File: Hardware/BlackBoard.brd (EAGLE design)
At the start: 68.6 x 53.3 mm, 78 parts, among them IC3 LM1117, J2 ISP, J3 POWER_JACKSUPER_BOMB_DIGITY, J5 USB C, Q1 1.1A/60V/600mΩ, Q2 310mA/60V/1.6Ω, Q3 310mA/60V/1.6Ω, U3 AP2112-3.3V, U4 ATMEGA328P_TQFP, U5 CH340C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

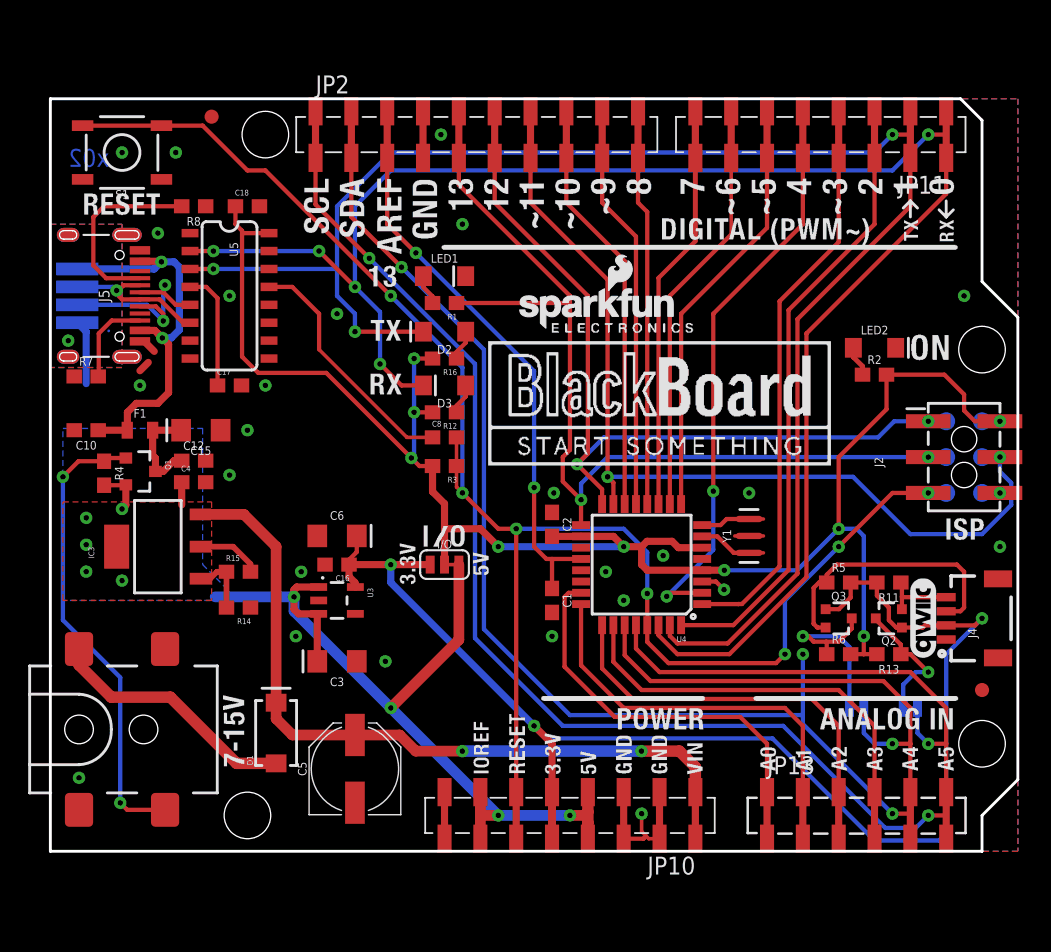
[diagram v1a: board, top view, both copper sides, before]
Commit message: Swap to larger PTC. Correct connection to IOREF.
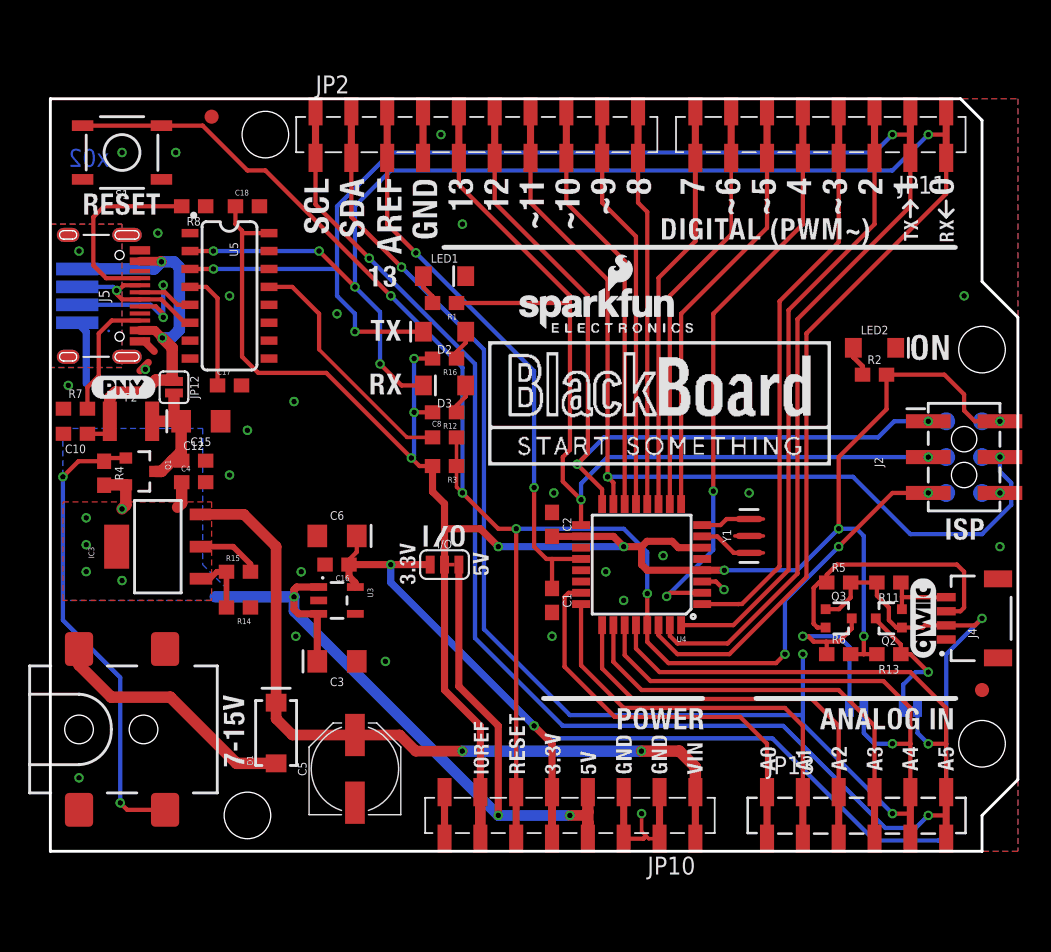
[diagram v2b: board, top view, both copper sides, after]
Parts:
- removed F1: 6V 0.5A, SparkFun-Fuses:0805
- added F2: 6V_2A, SparkFun-Fuses:1210
- added JP12: (no value), SparkFun-Jumpers:SMT-JUMPER_2_NO_SILK
- added U$13: (no value), buzzard_labels:PNY0
- J4: device SparkFun-Connectors:1X04_1MM_RA -> SparkFun-Connectors:JST04_1MM_RA
- moved R7 2.41 mm to (1.78, 31.4)
- moved C10 0.80 mm to (1.78, 29.6)
- moved C15 0.64 mm to (10.7, 30.5)
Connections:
- net 5V: no longer JP10.7A, JP10.7B
- net USBVCC: now also F2.2, JP12.2; no longer F1.2
- net VCC: now also JP10.7A, JP10.7B
- net VUSB: now also F2.1, JP12.1; no longer F1.1
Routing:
- net VCC: track 123.6 -> 144.1 mm
- net CC2: track 6.36 -> 8.97 mm
- net 5V: track 73.8 -> 76.3 mm, vias 9 -> 8
- net USBVCC: track 7.20 -> 9.50 mm
- net VUSB: track 27.7 -> 29.4 mm
- net D+: track 16.0 -> 15.4 mm
- net GND: track 12.9 -> 12.6 mm, vias 26 -> 27

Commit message: Adding panel
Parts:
- F2: value 6V_2A -> 6V/2A
- moved U$12 0.92 mm to (5.46, 42.0)
- moved U$11 0.85 mm to (5.46, 36.7)
- moved U$10 0.28 mm to (5.46, 40.3)
- moved U$2 0.25 mm to (5.59, 38.5)
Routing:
- net 5V: track 76.3 -> 76.8 mm
- net GND: track 12.6 -> 12.2 mm, vias 27 -> 42
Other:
- board text added: "x03"
- board text removed: "x02"

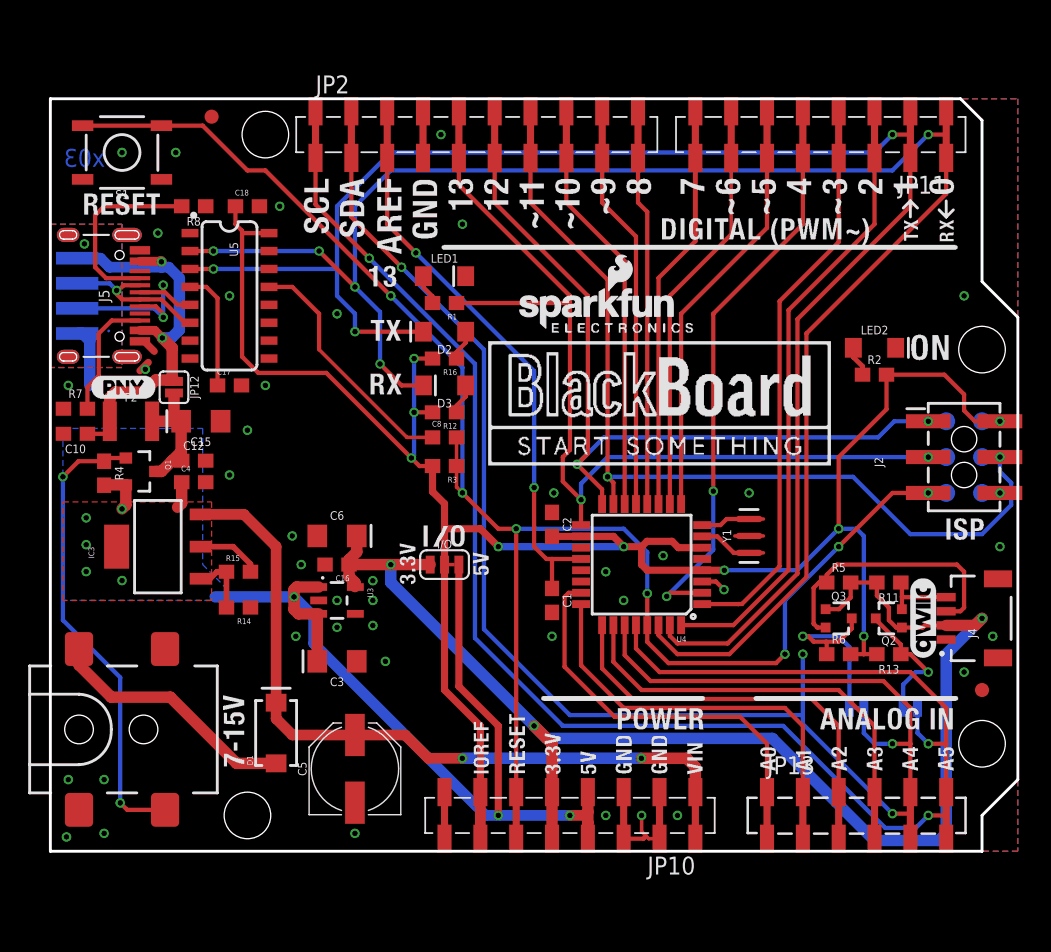
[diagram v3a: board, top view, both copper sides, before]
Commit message: Add switch for IO voltage. Add PTH holes.
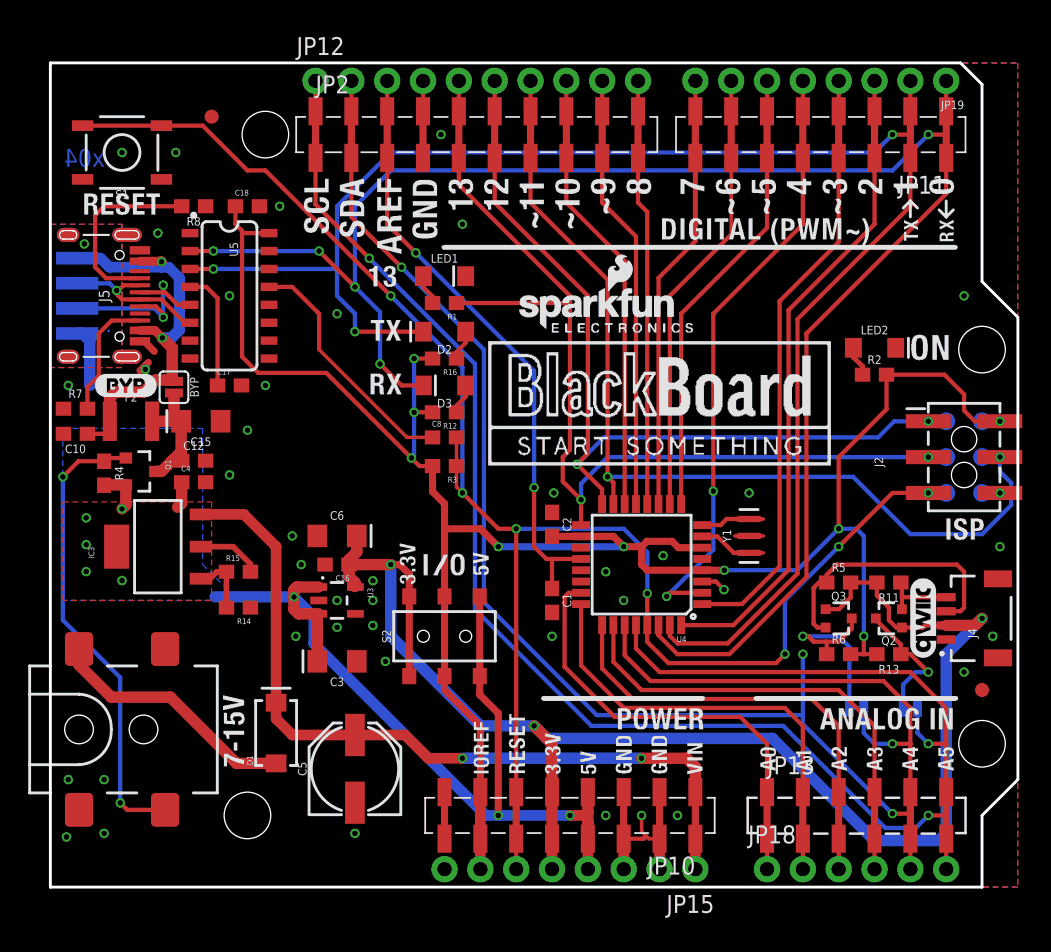
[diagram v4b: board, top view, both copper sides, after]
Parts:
- removed I/O: (no value), SparkFun-Jumpers:SMT-JUMPER_3_1-NC_TRACE_SILK
- removed U$13: (no value), buzzard_labels:PNY0
- added BYP: JUMPER-SMT_2_NO_SILK, SparkFun-Jumpers:SMT-JUMPER_2_NO_SILK
- added JP15: (no value), SparkFun-Connectors:1X08_NO_SILK@1
- added JP18: (no value), SparkFun-Connectors:1X06_NO_SILK@1
- added JP19: (no value), SparkFun-Connectors:1X08_NO_SILK
- added S2: (no value), SparkFun-Switches:SWITCH_DPDT_SMD_AYZ0202
- added U$68: (no value), buzzard_labels (13):BYP0
- D3: value Yellow -> YELLOW
- FRAME1: value FRAME-LETTER -> FRAME-LEDGER
- J4: value (none) -> QWIIC_RIGHT_ANGLE
- JP10, JP11: device SparkFun-Connectors:1X08_SMD_COMBINED -> SparkFun-Connectors:1X08_SMD_COMBINED@1
- JP12: value (none) -> M10NO_SILK; device SparkFun-Jumpers:SMT-JUMPER_2_NO_SILK -> SparkFun-Connectors:1X10_NO_SILK
- QW1, QW2: value (none) -> JUMPER-SMT_2_NC_TRACE_SILK
- moved JP12 23.9 mm to (18.8, 54.6), turned to 0 degrees
- moved FRAME1 2.54 mm to (-5.08, -35.6)
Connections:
- removed net AD0: JP13.1A, JP13.1B, U4.23
- removed net AD1: JP13.2A, JP13.2B, U4.24
- removed net AD2: JP13.3A, JP13.3B, U4.25
- removed net AD3: JP13.4A, JP13.4B, U4.26
- removed net AD4/SDA: JP13.5A, JP13.5B, JP2.2A, JP2.2B, QW2.1, U4.27
- removed net AD5/SCL: JP13.6A, JP13.6B, JP2.1A, JP2.1B, QW1.1, U4.28
- removed net IO2: JP11.3A, JP11.3B, U4.32
- removed net IO3: JP11.4A, JP11.4B, U4.1
- removed net IO4: JP11.5A, JP11.5B, U4.2
- removed net IO5: JP11.6A, JP11.6B, U4.9
- removed net IO6: JP11.7A, JP11.7B, U4.10
- removed net IO7: JP11.8A, JP11.8B, U4.11
- removed net IO8: JP2.10A, JP2.10B, U4.12
- removed net IO9: JP2.9A, JP2.9B, U4.13
- removed net RESET: C8.2, J2.5, JP10.6A, JP10.6B, R3.1, S1.3, S1.4, TP6.P$1, U4.29
- removed net SS: JP2.8A, JP2.8B, U4.14
- new net !RESET: C8.2, J2.5, JP10.6A, JP10.6B, JP15.6, R3.1, S1.3, S1.4, TP6.P$1, U4.29
- new net A0: JP13.1A, JP13.1B, JP18.1, U4.23
- new net A1: JP13.2A, JP13.2B, JP18.2, U4.24
- new net A2: JP13.3A, JP13.3B, JP18.3, U4.25
- new net A3: JP13.4A, JP13.4B, JP18.4, U4.26
- new net A4/SDA: JP12.2, JP13.5A, JP13.5B, JP18.5, JP2.2A, JP2.2B, QW2.1, U4.27
- new net A5/SCL: JP12.1, JP13.6A, JP13.6B, JP18.6, JP2.1A, JP2.1B, QW1.1, U4.28
- new net D10: JP12.8, JP2.8A, JP2.8B, U4.14
- new net D2: JP11.3A, JP11.3B, JP19.3, U4.32
- new net D3: JP11.4A, JP11.4B, JP19.4, U4.1
- new net D4: JP11.5A, JP11.5B, JP19.5, U4.2
- new net D5: JP11.6A, JP11.6B, JP19.6, U4.9
- new net D6: JP11.7A, JP11.7B, JP19.7, U4.10
- new net D7: JP11.8A, JP11.8B, JP19.8, U4.11
- new net D8: JP12.10, JP2.10A, JP2.10B, U4.12
- new net D9: JP12.9, JP2.9A, JP2.9B, U4.13
- net 3.3V: now also JP15.5, S2.1, S2.4; no longer I/O.1
- net 5V: now also JP15.4, S2.3, S2.6; no longer I/O.3
- net AREF: now also JP12.3
- net GND: now also JP12.4, JP15.2, JP15.3
- net MISO: now also JP12.6
- net MOSI: now also JP12.7
- net RX-I: now also JP19.1
- net SCK: now also JP12.5
- net TX-O: now also JP19.2
- net USBVCC: now also BYP.2; no longer JP12.2
- net VCC: now also JP15.7, S2.2, S2.5; no longer I/O.2
- net VIN: now also JP15.1
- net VUSB: now also BYP.1; no longer JP12.1
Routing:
- net A4/SDA: track 0.00 -> 124.2 mm, vias 0 -> 4
- net A5/SCL: track 0.00 -> 123.7 mm, vias 0 -> 3
- net !RESET: track 0.00 -> 121.4 mm, vias 0 -> 7
- net AD4/SDA: track 121.0 -> 0.00 mm, vias 4 -> 0
- net AD5/SCL: track 120.2 -> 0.00 mm, vias 3 -> 0
- net RESET: track 119.2 -> 0.00 mm, vias 7 -> 0
- net D2: track 0.00 -> 46.4 mm
- net IO2: track 44.3 -> 0.00 mm
- net D3: track 0.00 -> 43.6 mm
- net D4: track 0.00 -> 43.2 mm, vias 0 -> 2
- net IO3: track 41.5 -> 0.00 mm
- net IO4: track 41.0 -> 0.00 mm, vias 2 -> 0
- net A0: track 0.00 -> 35.0 mm
- net A2: track 0.00 -> 34.6 mm
- net A3: track 0.00 -> 33.1 mm
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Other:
- board size 68.6 x 53.3 mm -> 68.6 x 58.4 mm
- board text added: "x04"
- board text removed: "x03"
